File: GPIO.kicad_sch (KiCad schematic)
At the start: 0 parts

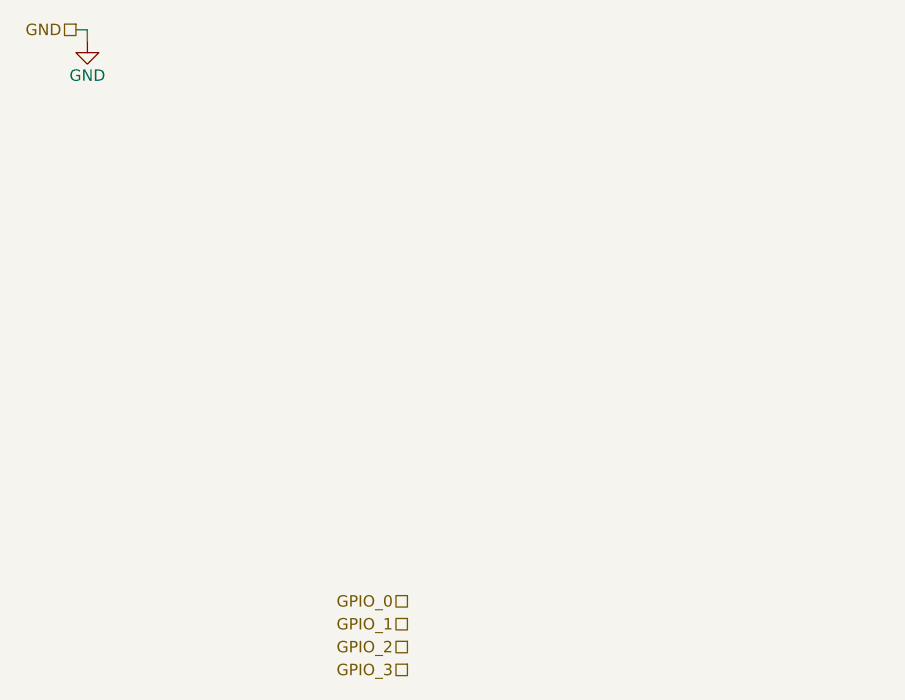
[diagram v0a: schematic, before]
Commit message: added 3.3v gpio input protection
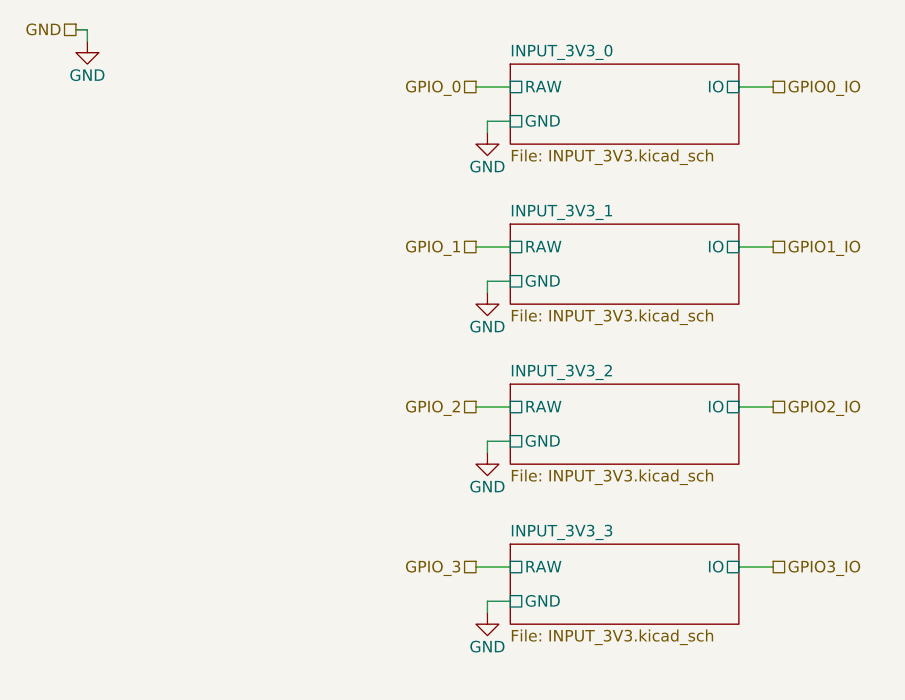
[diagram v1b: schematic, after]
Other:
- added sheet INPUT_3V3_0 (INPUT_3V3.kicad_sch)
- added sheet INPUT_3V3_1 (INPUT_3V3.kicad_sch)
- added sheet INPUT_3V3_2 (INPUT_3V3.kicad_sch)
- added sheet INPUT_3V3_3 (INPUT_3V3.kicad_sch)
